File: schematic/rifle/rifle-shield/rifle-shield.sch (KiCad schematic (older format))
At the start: 55 parts, among them K1 CONN_3, K2 CONN_3, P1 USB, P10 MCU2, P12 NRF24L01, P13 IR_LED, P15 Vibro&flash, P2 MCU1, P3 Mag&fireMode, P4 VCC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

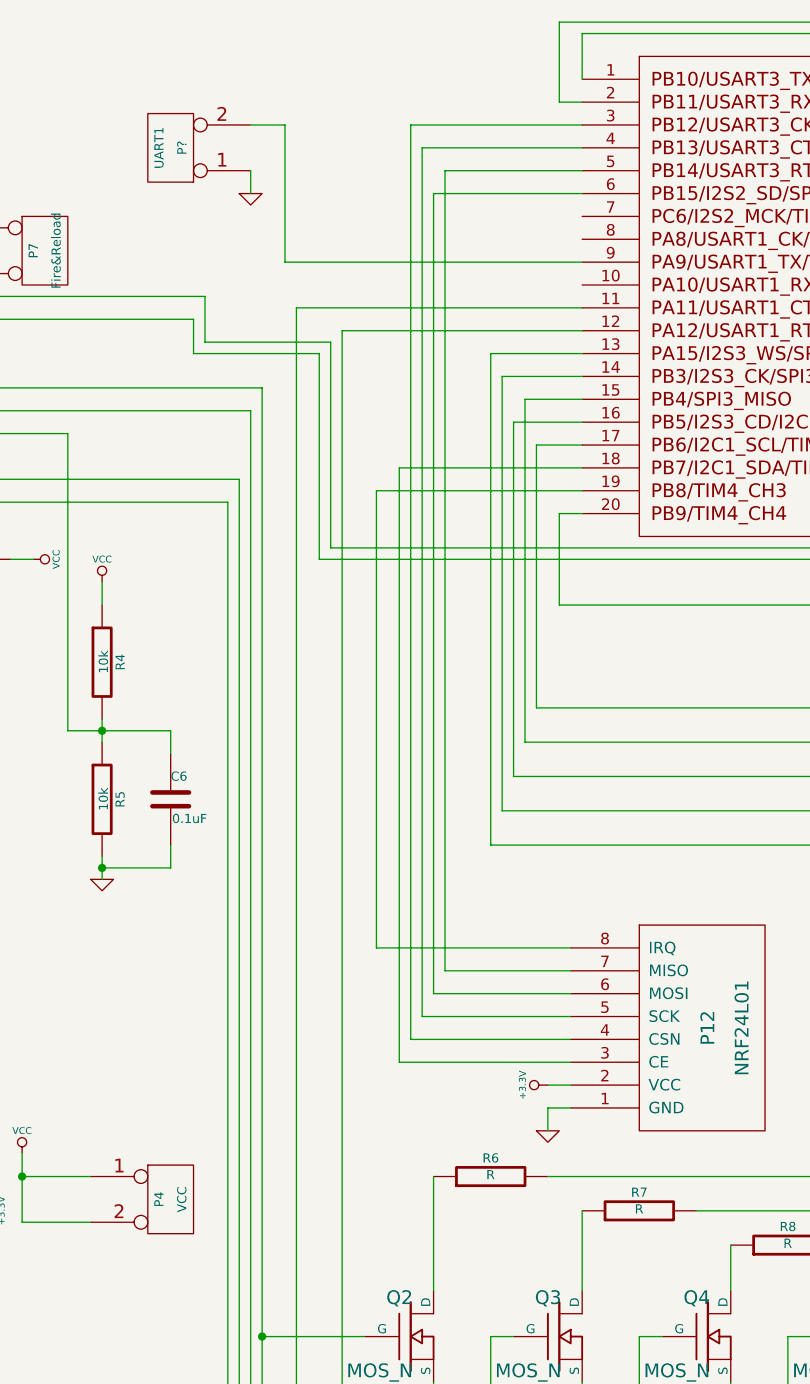
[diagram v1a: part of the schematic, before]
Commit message: Some rifle pcb improvements: led is 1206, tants are type E, hw rf swith added
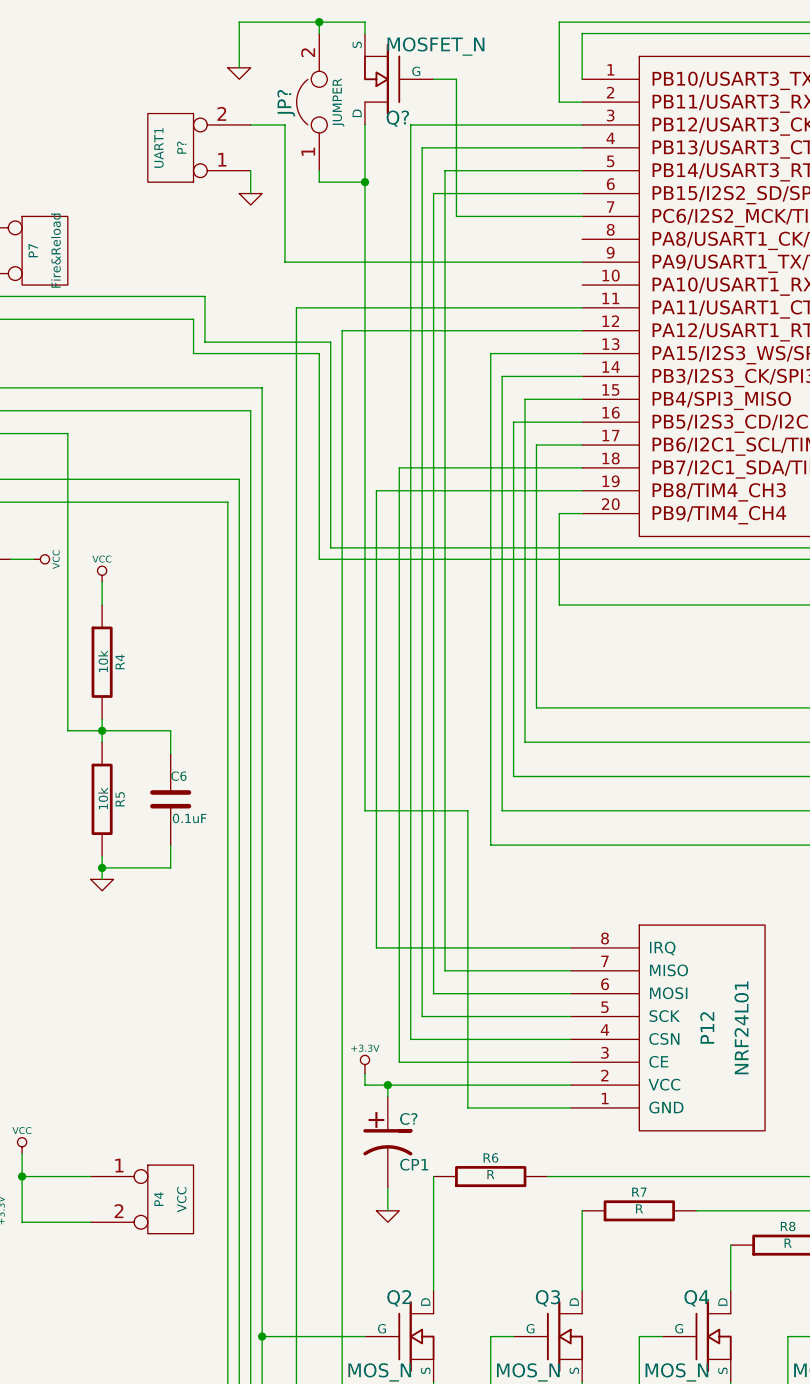
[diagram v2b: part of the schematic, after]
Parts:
- added C?: CP1, ~, symbol CP1
- added JP?: JUMPER, ~, symbol JUMPER
- added Q?: MOSFET_N, ~, symbol MOSFET_N
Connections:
- wire segments 244 -> 258
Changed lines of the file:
@@
 Sheet 1 1
 Title "Caustic lasertag system rifle shield"
-Date "20 jan 2016"
+Date "13 apr 2016"
 Rev "4"
 Comp ""
@@
 $EndComp
 $Comp
-L GND #PWR05
-U 1 1 556D6CFE
-P 7750 5400
-F 0 "#PWR05" H 7750 5400 30  0001 C CNN
-F 1 "GND" H 7750 5330 30  0001 C CNN
-F 2 "" H 7750 5400 60  0000 C CNN
-F 3 "" H 7750 5400 60  0000 C CNN
-	1    7750 5400
-	1    0    0    -1
-$EndComp
-$Comp
 L +3.3V #PWR06
 U 1 1 556D6D28
-P 7750 5200
-F 0 "#PWR06" H 7750 5160 30  0001 C CNN
-F 1 "+3.3V" H 7750 5310 30  0000 C CNN
-F 2 "" H 7750 5200 60  0000 C CNN
-F 3 "" H 7750 5200 60  0000 C CNN
-	1    7750 5200
-	0    -1   -1   0
+P 6950 5150
+F 0 "#PWR06" H 6950 5110 30  0001 C CNN
+F 1 "+3.3V" H 6950 5260 30  0000 C CNN
+F 2 "" H 6950 5150 60  0000 C CNN
+F 3 "" H 6950 5150 60  0000 C CNN
+	1    6950 5150
+	1    0    0    -1
 $EndComp
 $Comp
@@
 	7850 4700 7300 4700
 Wire Wire Line
-	7750 5200 7850 5200
-Wire Wire Line
-	7750 5300 7850 5300
-Wire Wire Line
-	7750 5400 7750 5300
+	6950 5200 7850 5200
 Wire Wire Line
 	7700 2400 7900 2400
@@
 Wire Wire Line
 	6450 1200 6450 1300
+$Comp
+L CP1 C?
+U 1 1 570D58F2
+P 7050 5450
+F 0 "C?" H 7100 5550 50  0000 L CNN
+F 1 "CP1" H 7100 5350 50  0000 L CNN
+F 2 "~" H 7050 5450 60  0000 C CNN
+F 3 "~" H 7050 5450 60  0000 C CNN
+	1    7050 5450
+	1    0    0    -1
+$EndComp
+$Comp
+L GND #PWR?
+U 1 1 570DE656
+P 7050 5750
+F 0 "#PWR?" H 7050 5750 30  0001 C CNN
+F 1 "GND" H 7050 5680 30  0001 C CNN
+F 2 "" H 7050 5750 60  0000 C CNN
+F 3 "" H 7050 5750 60  0000 C CNN
+	1    7050 5750
+	1    0    0    -1
+$EndComp
+Wire Wire Line
+	7050 5650 7050 5750
+Wire Wire Line
+	6950 5200 6950 5150
+Wire Wire Line
+	7050 5250 7050 5200
+Connection ~ 7050 5200
+$Comp
+L MOSFET_N Q?
+U 1 1 570DEF97
+P 7050 800
+F 0 "Q?" H 7060 970 60  0000 R CNN
+F 1 "MOSFET_N" H 7060 650 60  0000 R CNN
+F 2 "~" H 7050 800 60  0000 C CNN
+F 3 "~" H 7050 800 60  0000 C CNN
+	1    7050 800
+	-1   0    0    1
+$EndComp
+$Comp
+L GND #PWR?
+U 1 1 570DEFB3
+P 6400 750
+F 0 "#PWR?" H 6400 750 30  0001 C CNN
+F 1 "GND" H 6400 680 30  0001 C CNN
+F 2 "" H 6400 750 60  0000 C CNN
+F 3 "" H 6400 750 60  0000 C CNN
+	1    6400 750
+	1    0    0    -1
+$EndComp
+$Comp
+L JUMPER JP?
+U 1 1 570DEFE4
+P 6750 900
+F 0 "JP?" H 6750 1050 60  0000 C CNN
+F 1 "JUMPER" H 6750 820 40  0000 C CNN
+F 2 "~" H 6750 900 60  0000 C CNN
+F 3 "~" H 6750 900 60  0000 C CNN
+	1    6750 900
+	0    -1   -1   0
+$EndComp
+Wire Wire Line
+	6400 750  6400 550
+Wire Wire Line
+	6400 550  6950 550
+Wire Wire Line
+	6950 550  6950 600
+Wire Wire Line
+	6750 600  6750 550
+Connection ~ 6750 550
+Wire Wire Line
+	6750 1200 6750 1250
+Wire Wire Line
+	6750 1250 6950 1250
+Wire Wire Line
+	6950 1000 6950 4000
+Wire Wire Line
+	7850 5300 7400 5300
+Wire Wire Line
+	7400 5300 7400 4000
+Wire Wire Line
+	7400 4000 6950 4000
+Connection ~ 6950 1250
+Wire Wire Line
+	7900 1400 7350 1400
+Wire Wire Line
+	7350 1400 7350 800
+Wire Wire Line
+	7350 800  7250 800
 $EndSCHEMATC
